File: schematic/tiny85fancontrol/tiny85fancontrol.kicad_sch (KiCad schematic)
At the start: 11 parts, among them J1 UART_DBG, J2 Molex, M1 Fan, Q1 IRF3808, U1 ATtiny85-20P, U2 DS18B20

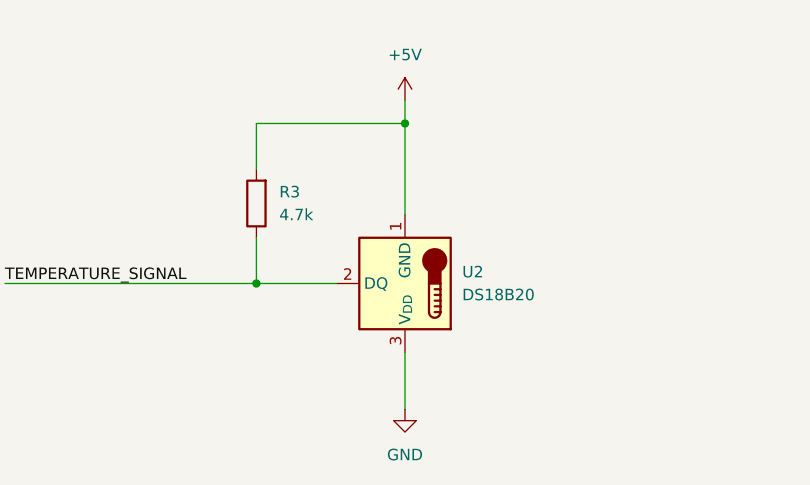
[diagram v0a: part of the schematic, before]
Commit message: Fix: Temperature sensor connected backwards
Thanks to amdj at #kicad for spotting this issue
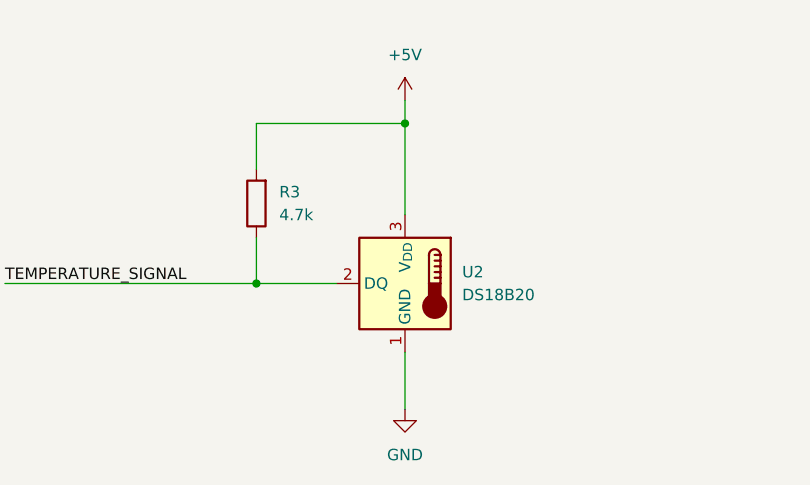
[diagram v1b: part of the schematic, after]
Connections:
- net +5V: now also U2.3 (V_{DD}); no longer U2.1 (GND)
- net GND: now also U2.1 (GND); no longer U2.3 (V_{DD})
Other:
- moved on the sheet: U2
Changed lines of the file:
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@@
 	(symbol
 		(lib_id "Sensor_Temperature:DS18B20")
-		(at 59.69 156.21 180)
+		(at 59.69 156.21 0)
+		(mirror y)
 		(unit 1)
 		(exclude_from_sim no)
@@
 		(on_board yes)
 		(dnp no)
-		(fields_autoplaced yes)
 		(property "Reference" "U2"
 			(at 66.04 154.9399 0)
@@
 		)
 		(property "Footprint" "Package_TO_SOT_THT:TO-92_Inline"
-			(at 85.09 149.86 0)
+			(at 85.09 162.56 0)
 			(effects
 				(font
@@
 		)
 		(property "Datasheet" "http://datasheets.maximintegrated.com/en/ds/DS18B20.pdf"
-			(at 63.5 162.56 0)
+			(at 63.5 149.86 0)
 			(effects
 				(font

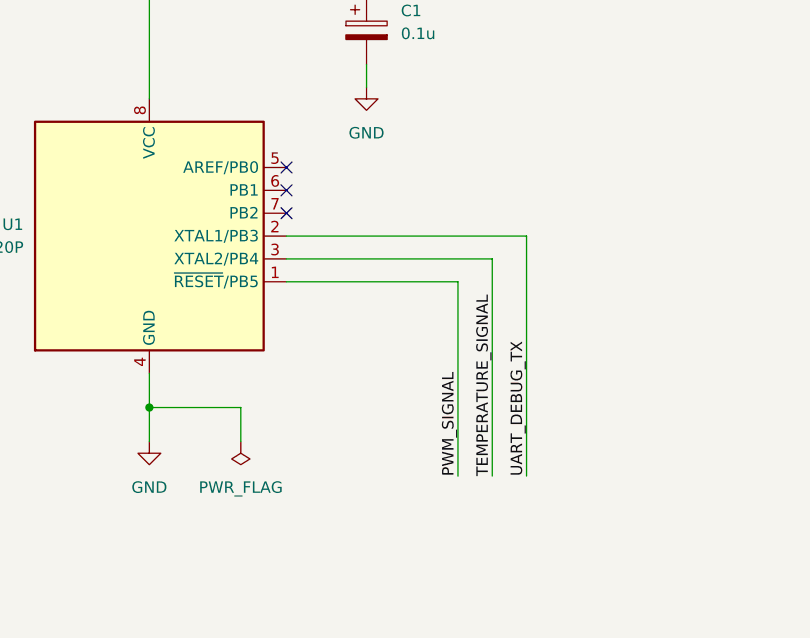
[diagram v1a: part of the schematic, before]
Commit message: Update Schematic and PCB According to Reviews
Placed temperature sensor away from MOSFET.
Fixed PIN assignments according to software.
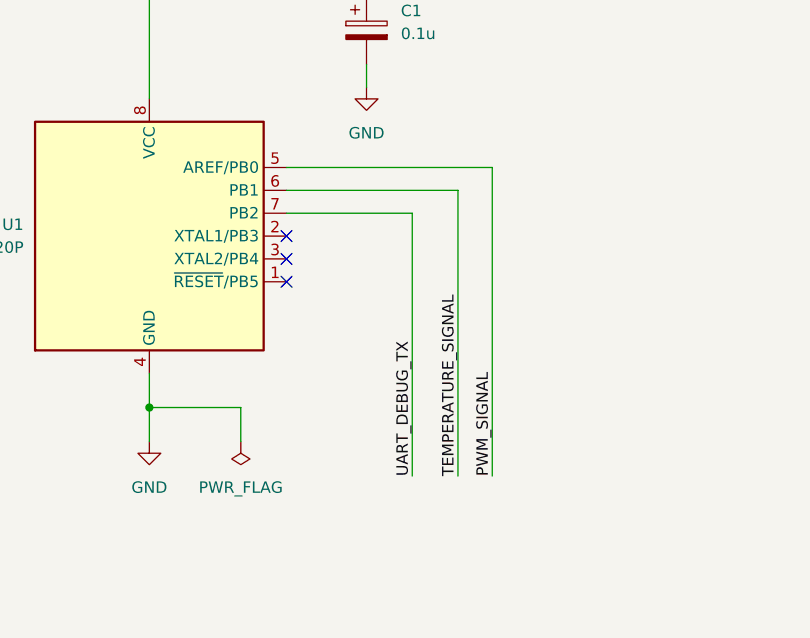
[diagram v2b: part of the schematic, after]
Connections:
- net PWM_SIGNAL: now also U1.5 (AREF/PB0); no longer U1.1 (~{RESET}/PB5)
- net TEMPERATURE_SIGNAL: now also U1.6 (PB1); no longer U1.3 (XTAL2/PB4)
- net UART_DEBUG_TX: now also U1.7 (PB2); no longer U1.2 (XTAL1/PB3)
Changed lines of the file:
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@@
 	)
 	(no_connect
-		(at 142.24 83.82)
+		(at 142.24 93.98)
 	)
 	(no_connect
-		(at 142.24 86.36)
+		(at 142.24 91.44)
 	)
 	(no_connect
-		(at 142.24 88.9)
+		(at 142.24 96.52)
 	)
 	(wire
@@
 	(wire
 		(pts
-			(xy 168.91 91.44) (xy 142.24 91.44)
-		)
-		(stroke
-			(width 0)
-			(type default)
-		)
-	)
-	(wire
-		(pts
 			(xy 210.82 128.27) (xy 228.6 128.27)
 		)
@@
 	(wire
 		(pts
+			(xy 156.21 88.9) (xy 156.21 118.11)
+		)
+		(stroke
+			(width 0)
+			(type default)
+		)
+	)
+	(wire
+		(pts
 			(xy 59.69 138.43) (xy 59.69 148.59)
 		)
@@
 	(wire
 		(pts
+			(xy 165.1 83.82) (xy 165.1 118.11)
+		)
+		(stroke
+			(width 0)
+			(type default)
+		)
+	)
+	(wire
+		(pts
 			(xy 236.22 34.29) (xy 236.22 30.48)
 		)
@@
 	(wire
 		(pts
+			(xy 142.24 86.36) (xy 161.29 86.36)
+		)
+		(stroke
+			(width 0)
+			(type default)
+		)
+	)
+	(wire
+		(pts
 			(xy 219.71 62.23) (xy 219.71 67.31)
 		)
@@
 	(wire
 		(pts
-			(xy 165.1 93.98) (xy 142.24 93.98)
-		)
-		(stroke
-			(width 0)
-			(type default)
-		)
-	)
-	(wire
-		(pts
 			(xy 219.71 34.29) (xy 236.22 34.29)
 		)
@@
 	(wire
 		(pts
+			(xy 161.29 86.36) (xy 161.29 118.11)
+		)
+		(stroke
+			(width 0)
+			(type default)
+		)
+	)
+	(wire
+		(pts
 			(xy 43.18 151.13) (xy 43.18 156.21)
 		)
@@
 	(wire
 		(pts
-			(xy 161.29 96.52) (xy 142.24 96.52)
-		)
-		(stroke
-			(width 0)
-			(type default)
-		)
-	)
-	(wire
-		(pts
 			(xy 40.64 53.34) (xy 40.64 49.53)
 		)
@@
 	(wire
 		(pts
-			(xy 165.1 118.11) (xy 165.1 93.98)
-		)
-		(stroke
-			(width 0)
-			(type default)
-		)
-	)
-	(wire
-		(pts
 			(xy 30.48 34.29) (xy 40.64 34.29)
 		)
@@
 	(wire
 		(pts
+			(xy 165.1 83.82) (xy 142.24 83.82)
+		)
+		(stroke
+			(width 0)
+			(type default)
+		)
+	)
+	(wire
+		(pts
 			(xy 40.64 49.53) (xy 30.48 49.53)
 		)
@@
 	(wire
 		(pts
+			(xy 142.24 88.9) (xy 156.21 88.9)
+		)
+		(stroke
+			(width 0)
+			(type default)
+		)
+	)
+	(wire
+		(pts
 			(xy 127 60.96) (xy 127 76.2)
 		)
@@
 		)
 	)
-	(wire
-		(pts
-			(xy 168.91 118.11) (xy 168.91 91.44)
-		)
-		(stroke
-			(width 0)
-			(type default)
-		)
-	)
-	(wire
-		(pts
-			(xy 161.29 118.11) (xy 161.29 96.52)
-		)
-		(stroke
-			(width 0)
-			(type default)
-		)
-	)
 	(label "TEMPERATURE_SIGNAL"
-		(at 165.1 118.11 90)
+		(at 161.29 118.11 90)
 		(effects
 			(font
@@
 	)
 	(label "PWM_SIGNAL"
-		(at 161.29 118.11 90)
+		(at 165.1 118.11 90)
 		(effects
 			(font
@@
 	)
 	(label "UART_DEBUG_TX"
-		(at 168.91 118.11 90)
+		(at 156.21 118.11 90)
 		(effects
 			(font
